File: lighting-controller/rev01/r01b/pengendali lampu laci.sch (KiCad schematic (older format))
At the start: 15 parts, among them M1 LM2596_Module, P1 Power, SW1 SPST

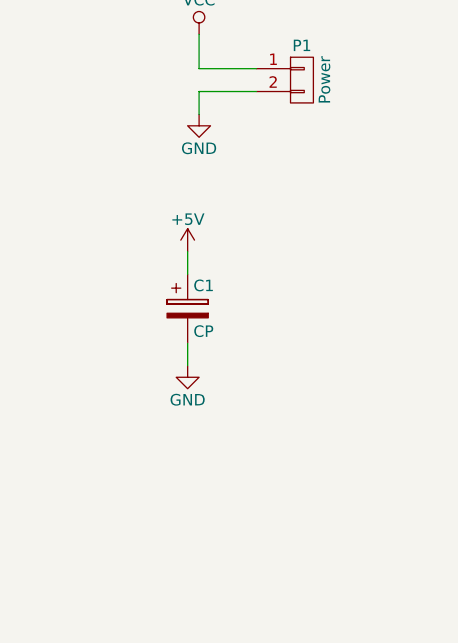
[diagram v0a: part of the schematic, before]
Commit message: Update controller
* Add led
* Use switch
* Use barrel jack
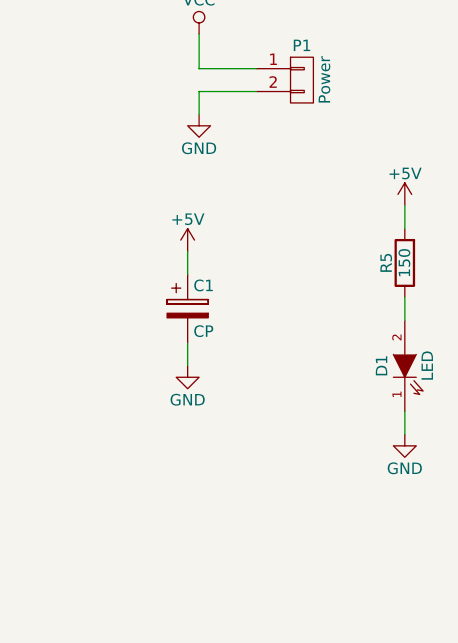
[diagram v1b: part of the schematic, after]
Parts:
- added D1: LED, LEDs:LED_1206, symbol LED
- added R5: 150, Resistors_SMD:R_1206_HandSoldering, symbol R
- P1: footprint Connect:bornier2 -> Connect:BARREL_JACK
- SW1: footprint Pin_Headers:Pin_Header_Straight_1x02 -> Buttons_Switches_ThroughHole:SW_Micro_SPST
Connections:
- net +5V: now also R5.2
- net GND: now also D1.1 (K)
- new net: D1.2 (A), R5.1
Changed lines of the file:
@@
 F 0 "P1" H 7250 2650 50  0000 C CNN
 F 1 "Power" V 7350 2500 50  0000 C CNN
-F 2 "Connect:bornier2" H 7250 2500 50  0001 C CNN
+F 2 "Connect:BARREL_JACK" H 7250 2500 50  0001 C CNN
 F 3 "" H 7250 2500 50  0000 C CNN
 	1    7250 2500
@@
 F 0 "SW1" H 4900 5150 50  0000 C CNN
 F 1 "SPST" H 4900 4950 50  0000 C CNN
-F 2 "Pin_Headers:Pin_Header_Straight_1x02" H 4900 5050 50  0001 C CNN
+F 2 "Buttons_Switches_ThroughHole:SW_Micro_SPST" H 4900 5050 50  0001 C CNN
 F 3 "" H 4900 5050 50  0000 C CNN
 	1    4900 5050
@@
 Wire Wire Line
 	5500 5050 5500 4950
+$Comp
+L GND #PWR024
+U 1 1 57D5D6E8
+P 7700 4050
+F 0 "#PWR024" H 7700 3800 50  0001 C CNN
+F 1 "GND" H 7700 3900 50  0000 C CNN
+F 2 "" H 7700 4050 50  0000 C CNN
+F 3 "" H 7700 4050 50  0000 C CNN
+	1    7700 4050
+	1    0    0    -1
+$EndComp
+$Comp
+L +5V #PWR025
+U 1 1 57D5D6F0
+P 7700 3050
+F 0 "#PWR025" H 7700 2900 50  0001 C CNN
+F 1 "+5V" H 7700 3190 50  0000 C CNN
+F 2 "" H 7700 3050 50  0000 C CNN
+F 3 "" H 7700 3050 50  0000 C CNN
+	1    7700 3050
+	1    0    0    -1
+$EndComp
+$Comp
+L LED D1
+U 1 1 57D5D708
+P 7700 3750
+F 0 "D1" H 7700 3850 50  0000 C CNN
+F 1 "LED" H 7700 3650 50  0000 C CNN
+F 2 "LEDs:LED_1206" H 7700 3750 50  0001 C CNN
+F 3 "" H 7700 3750 50  0000 C CNN
+	1    7700 3750
+	0    -1   -1   0
+$EndComp
+$Comp
+L R R5
+U 1 1 57D5E01D
+P 7700 3300
+F 0 "R5" V 7780 3300 50  0000 C CNN
+F 1 "150" V 7700 3300 50  0000 C CNN
+F 2 "Resistors_SMD:R_1206_HandSoldering" V 7630 3300 50  0001 C CNN
+F 3 "" H 7700 3300 50  0000 C CNN
+	1    7700 3300
+	-1   0    0    1
+$EndComp
+Wire Wire Line
+	7700 3050 7700 3150
+Wire Wire Line
+	7700 3450 7700 3550
+Wire Wire Line
+	7700 3950 7700 4050
 $EndSCHEMATC
